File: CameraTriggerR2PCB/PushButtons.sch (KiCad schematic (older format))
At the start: 8 parts, among them J10 Trig, J11 Arm, SW2 SW_Trigger, SW3 SW_Arm, SW4 SW_Poll

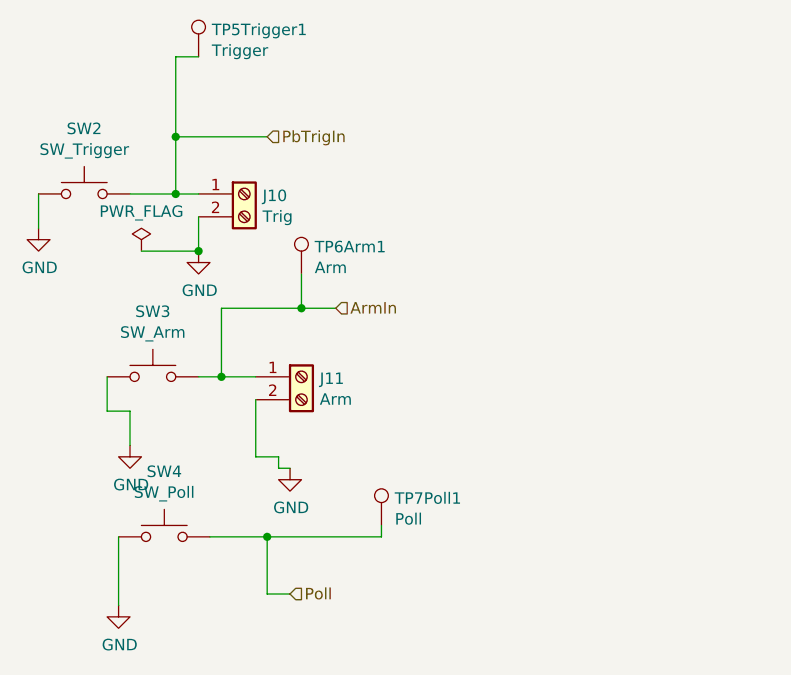
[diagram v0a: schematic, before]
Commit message: Add files via upload
Adding XLR connector
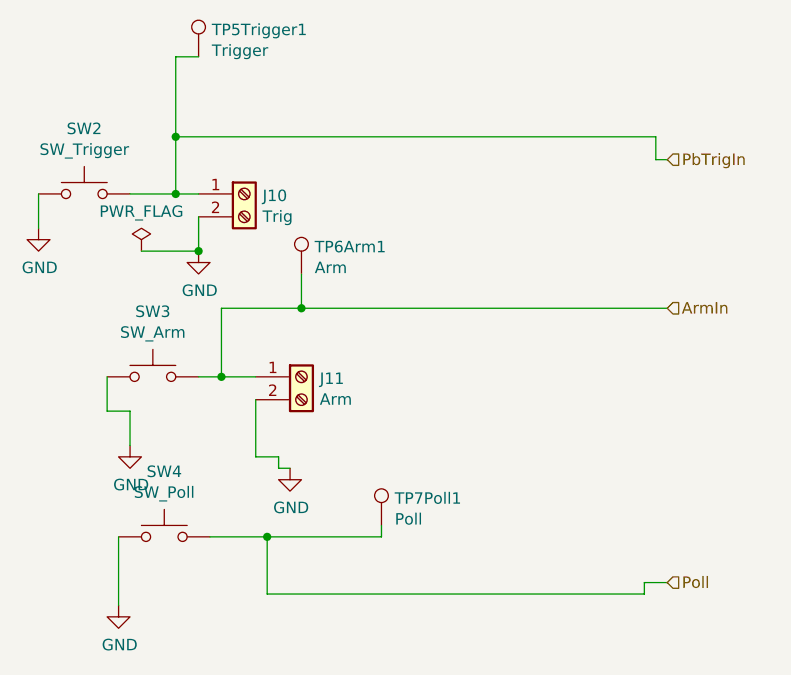
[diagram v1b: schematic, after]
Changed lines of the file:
@@
 $Descr A4 11693 8268
 encoding utf-8
-Sheet 5 8
+Sheet 5 9
 Title ""
 Date ""
@@
 	3900 2600 3900 2750
 Wire Wire Line
-	4200 4250 4300 4250
-Wire Wire Line
 	3550 4000 3550 4300
 Connection ~ 3800 2500
@@
 Wire Wire Line
 	3600 2500 3800 2500
-Wire Wire Line
-	3800 2250 4200 2250
 Wire Wire Line
 	3800 2250 3800 2500
@@
 Connection ~ 4350 3000
 Wire Wire Line
-	4350 3000 4500 3000
-Wire Wire Line
 	4150 3400 4150 3650
 Wire Wire Line
@@
 	3650 2750 3900 2750
 Connection ~ 3900 2750
-Text HLabel 4200 2250 2    50   Input ~ 0
+Text HLabel 5950 2350 2    50   Input ~ 0
 PbTrigIn
-Text HLabel 4500 3000 2    50   Input ~ 0
+Text HLabel 5950 3000 2    50   Input ~ 0
 ArmIn
-Text HLabel 4300 4250 2    50   Input ~ 0
+Text HLabel 5950 4200 2    50   Input ~ 0
 Poll
+Wire Wire Line
+	5900 2250 5900 2350
+Wire Wire Line
+	5900 2350 5950 2350
+Wire Wire Line
+	3800 2250 5900 2250
+Wire Wire Line
+	4350 3000 5950 3000
+Wire Wire Line
+	5850 4250 5850 4200
+Wire Wire Line
+	5850 4200 5950 4200
+Wire Wire Line
+	4200 4250 5850 4250
 $EndSCHEMATC
